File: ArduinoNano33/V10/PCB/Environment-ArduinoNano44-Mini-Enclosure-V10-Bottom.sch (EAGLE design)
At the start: 19 parts, among them IC1 BME680

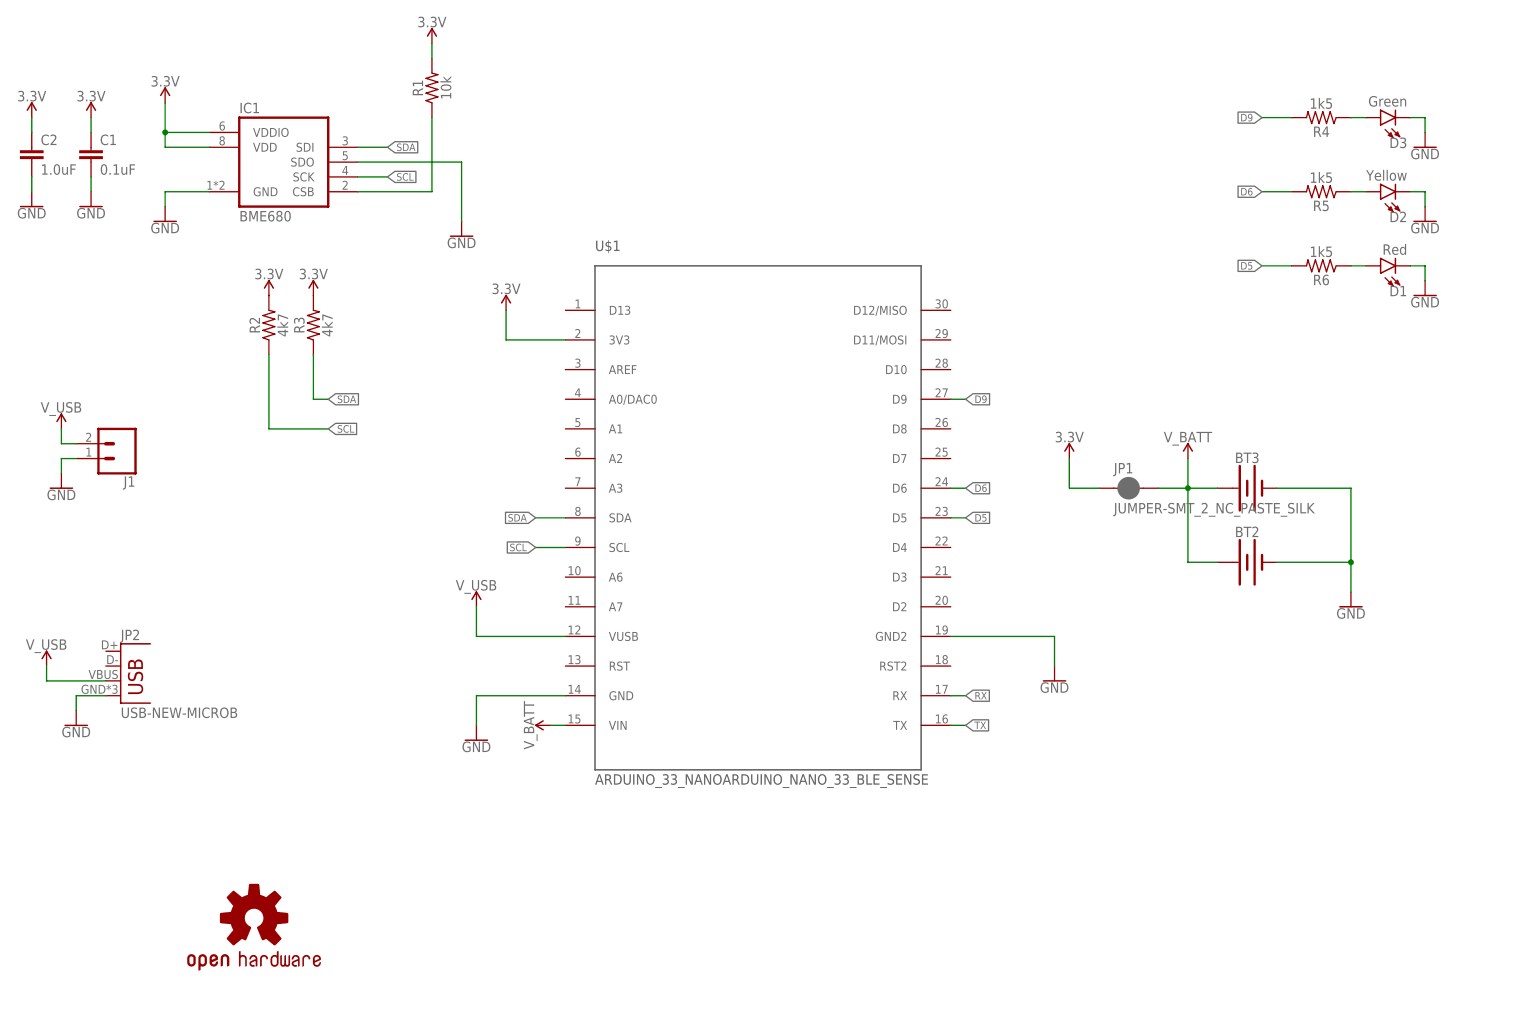
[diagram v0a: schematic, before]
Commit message: Split out personal environmental sensor boards into individual Eagle files.
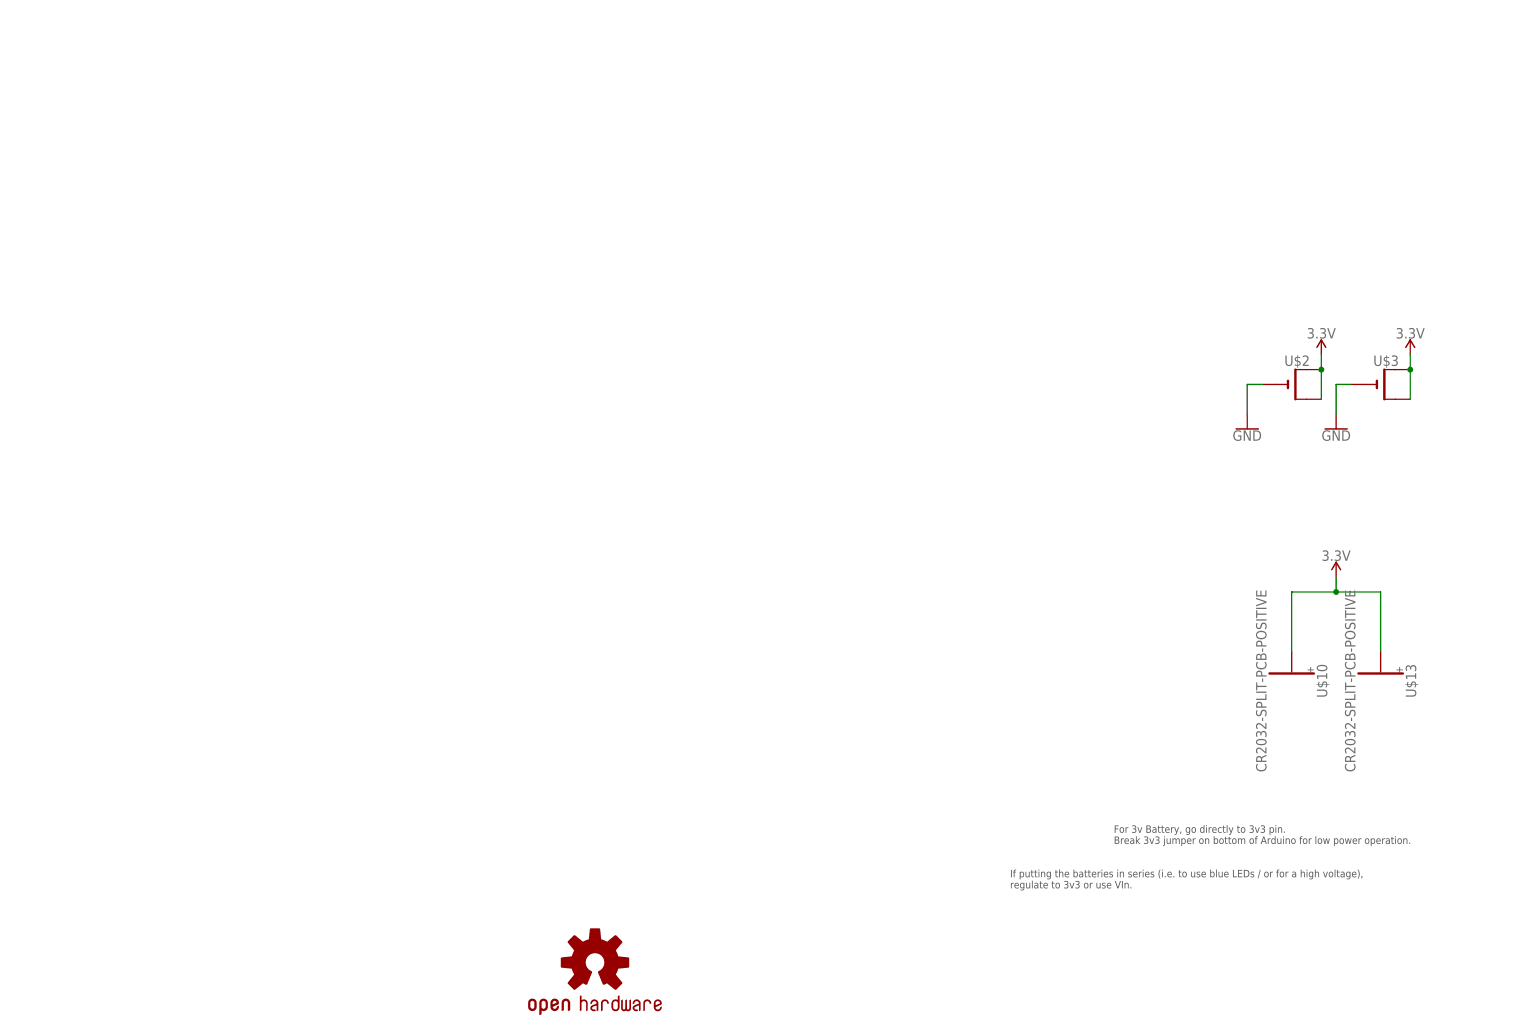
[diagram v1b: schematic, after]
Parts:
- removed BT2, BT3: (no value), ThingySticks:BATTERY-12MM_PTH
- removed C1: 0.1uF, ThingySticks:0.1UF-0805-25V
- removed C2: 1.0uF, ThingySticks:1.0UF-0805-25V-10%
- removed D1: Red, ThingySticks:LED1206
- removed D2: Yellow, ThingySticks:LED1206
- removed D3: Green, ThingySticks:LED1206
- removed IC1: BME680, ThingySticks:BME680
- removed J1: (no value), ThingySticks:CONN_02JST-2-PH-SIDE
- removed JP1: JUMPER-SMT_2_NC_PASTE_SILK, SparkFun-Jumpers:JUMPER-SMT_2_NC_PASTE_SILK
- removed JP2: USB-NEW-MICROB, Tinamous:USB-NEW-MICROB
- removed LOGO1: OSHW-LOGOM, SparkFun-Aesthetics:OSHW-LOGOM
- removed R1: 10k, SparkFun-Resistors:RESISTOR0805
- removed R2, R3: 4k7, SparkFun-Resistors:RESISTOR0805
- removed R4, R5, R6: 1k5, SparkFun-Resistors:RESISTOR0805
- removed U$1: ARDUINO_33_NANOARDUINO_NANO_33_BLE_SENSE, ThingySticks:ARDUINO_33_NANOARDUINO_NANO_33_BLE_SENSE
- added LOGO3: OSHW-LOGOL, SparkFun-Aesthetics:OSHW-LOGOL
- added U$10, U$13: CR2032-SPLIT-PCB-POSITIVE, ThingySticks:CR2032-SPLIT-PCB-POSITIVE
- added U$2, U$3: (no value), ThingySticks:CR2032SMT
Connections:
- removed net D5: R6.2, U$1.D5
- removed net D6: R5.2, U$1.D6
- removed net D9: R4.2, U$1.D9
- removed net N$10: D1.A, R6.1
- removed net N$2: IC1.CSB, R1.1
- removed net N$8: D3.A, R4.1
- removed net N$9: D2.A, R5.1
- removed net RX: U$1.RX
- removed net SCL: IC1.SCK, R2.1, U$1.SCL
- removed net SDA: IC1.SDI, R3.1, U$1.SDA
- removed net TX: U$1.TX
- removed net V_BATT: BT2.+, BT3.+, JP1.2, U$1.VIN
- removed net V_USB: J1.1, JP2.VBUS, U$1.VUSB
- net 3.3V: now also U$10.+, U$13.+, U$2.+, U$2.+1, U$3.+, U$3.+1; no longer C1.1, C2.1, IC1.VDD, IC1.VDDIO, JP1.1, R1.2, R2.2, R3.2, U$1.3V3
- net GND: now also U$2.-, U$3.-; no longer BT2.-, BT3.-, C1.2, C2.2, D1.C, D2.C, D3.C, IC1.GND, IC1.SDO, J1.2, JP2.GND, U$1.GND, U$1.GND2
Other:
- note added: "For 3v Battery, go directly to 3v3 pin. Break 3v3 jumper on bottom of Arduino for low power operation."
- note added: "If putting the batteries in series (i.e. to use blue LEDs / or for a high voltage), regulate to 3v3 or use VIn."
- note removed: "// Low power notes: // MP34DT05-A 1.6 - 3.6V. Tyical 1.8 (Mic) // LSM9DS3 1.9 V to 3.6 V (Accel) // APDS9960 2.4 - 3.6 (Typical 3.0) (Light) // LPS22HB 1.7 to 3.6 V (Pressure) // HTS221 1.7 to 3.6 V (Temperature / Humidity) // NINA-B3 1.7 to 3.6 (Typical 3.3) // DL3 - R + G + B LED (Blue won't work at 3v) // Extra... // BME680 1.71 to 3.6"
- note removed: "Arduino CPU: 4.2.3 Current consumption Table 14 shows the typical current consumption of a NINA-B3 module, independent of the software used. Mode Condition Typical Peak Sleep No clocks running, no RAM data retention 400 nA Sleep No clocks running, 64 kB RAM data retention 880 nA Sleep No clocks running, 256 kB RAM data retention 2.3 µA Standby RTC and 64 kB RAM data retention. System running on 3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"
- note removed: "CR2032: 3.0V, 210mAh Dropoff voltage, 2.5-2.0 Max current: 10mA CR2450: 15mA CR2016: 10mA CR1225: 3.0V, 48mAG Max 1.0mA"
- note removed: "Drive strngth. VCC >=2.7V Min 6, max 14ma. Typical 9mA"
- note removed: "Notes: Arduino has RGB LED. Do we need D1..D3. They could be right angle to project onto wall / floor / ceiling? Arduino needs 3v3 jumper broken on base - won't then use regulator to supply 3v3 so needs power (will battery work?) Add diode to batterys and direct to 3v3 supply, don't use VIN (V_BATT). V_IN will be disconnected Add option for external 3v3 supply (JST - bit not LiPol battery!) Remov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"
